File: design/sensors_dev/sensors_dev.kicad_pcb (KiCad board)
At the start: 2 copper layers, 58.9 x 36.6 mm, 44 parts, among them J1 Conn_01x02, J2 Conn_01x05, J4 Conn_01x12, Q1 RE1C002UN, Q2 RE1C002UN, U1 LP2980AIM5-3.0, U2 BMC150, U3 LSM6DS3HTR, U4 BMG250, U5 MS5607-02BA03, U6 LIS3DHTR

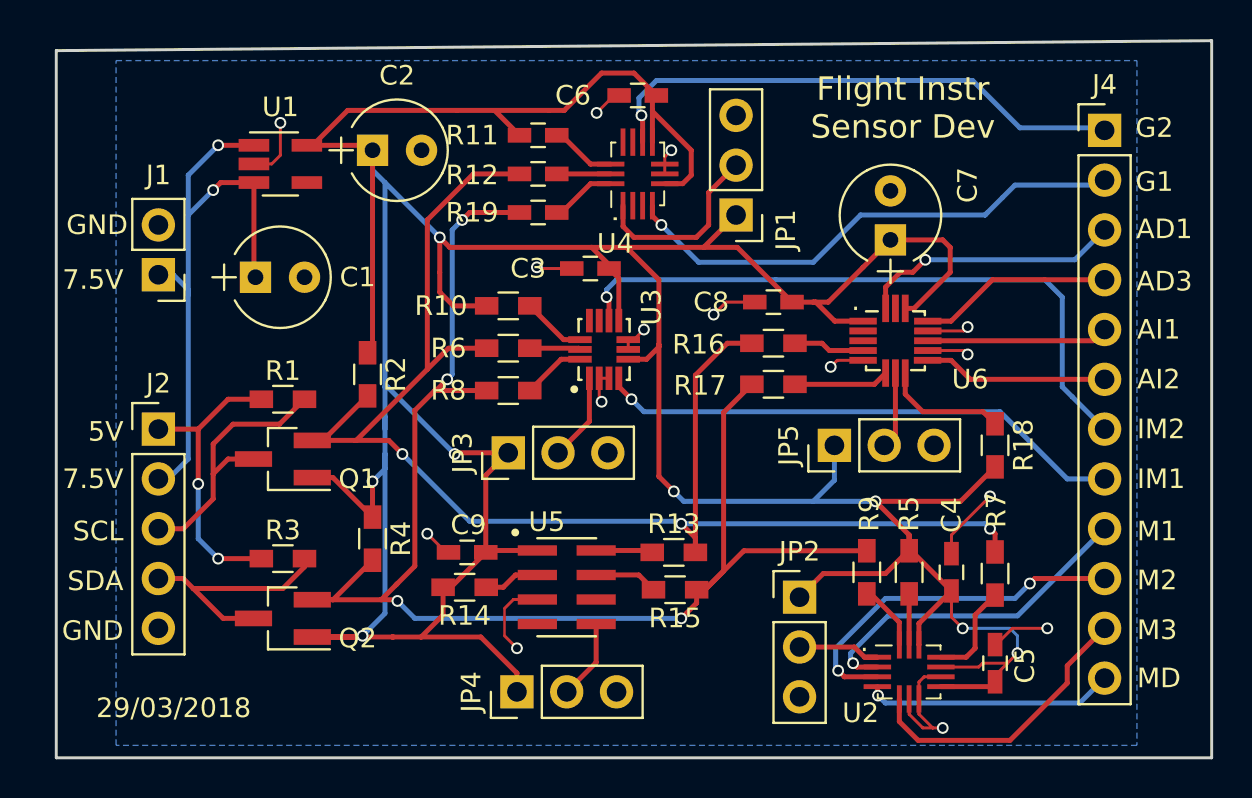
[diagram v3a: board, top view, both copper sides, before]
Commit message: Minor review changes
Move C9 and R14 further away from U5.
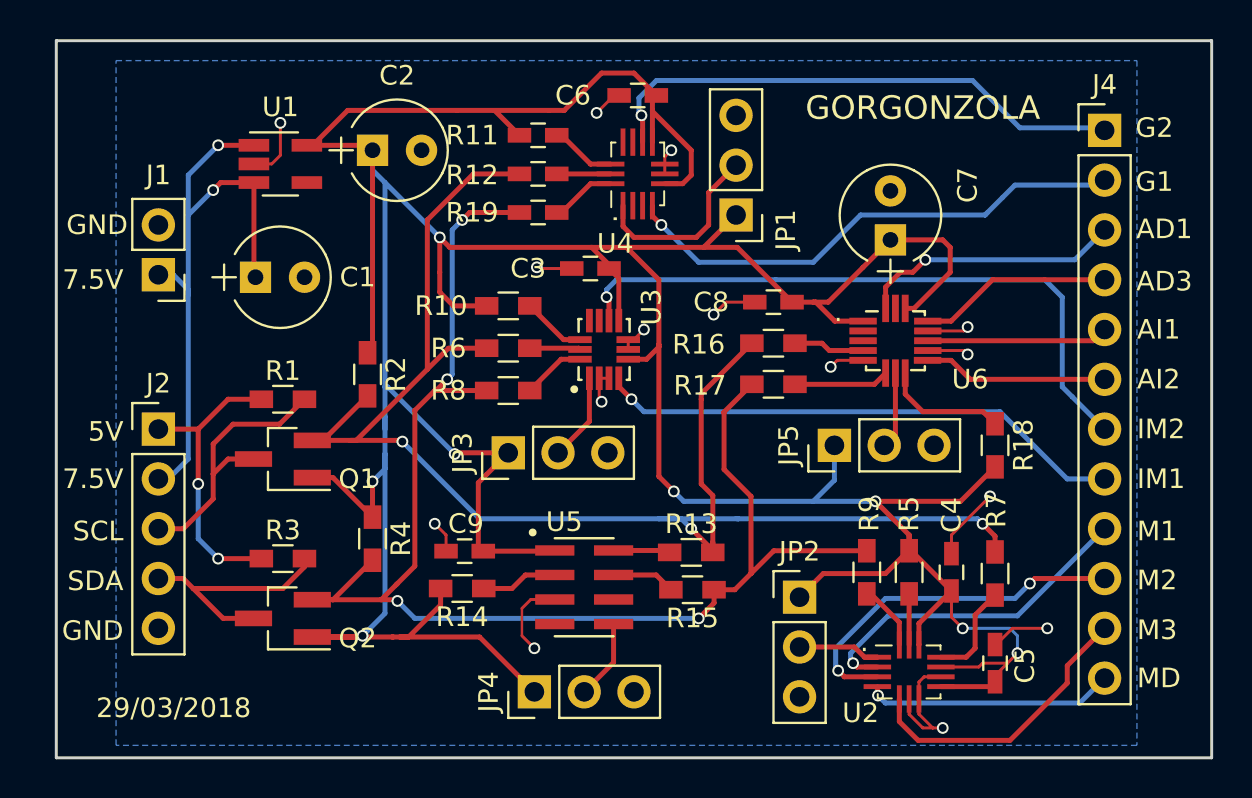
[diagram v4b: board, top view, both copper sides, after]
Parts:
- moved JP4 0.89 mm to (119.5, 147.0)
- moved R13 0.89 mm to (127.5, 139.9)
- moved R15 0.89 mm to (127.6, 141.8)
- moved U5 0.89 mm to (122.0, 141.7)
- moved C9 0.14 mm to (116.0, 139.8)
- moved R14 0.14 mm to (115.8, 141.7)
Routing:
- net SCL_3V: track 77.8 -> 79.7 mm
- net Net-(R14-Pad1): track 2.87 -> 3.91 mm
- net +3.0V: track 236.4 -> 235.6 mm
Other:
- outline, holes or cut-outs redrawn
- board text added: "GORGONZOLA"
- board text removed: "Flight Instr Sensor Dev"
